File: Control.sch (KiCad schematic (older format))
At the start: 4 parts, among them J1 Conn_01x03_Female, J2 Conn_01x02_Female, U1 WeMos_mini, U19 BME280

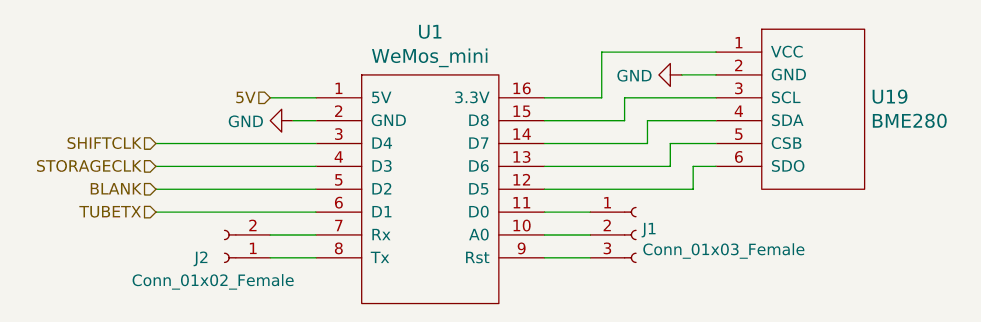
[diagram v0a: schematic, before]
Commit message: Fixed tube footprints and rerouted
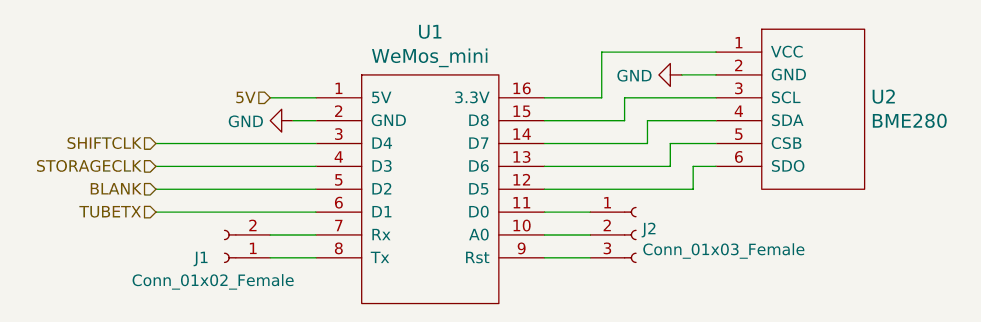
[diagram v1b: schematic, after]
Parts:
- U1: footprint BamboulabFootprints:D1_mini_board -> Bamboulibs:D1_mini_board
- renumbered J2 to J1, J1 to J2, U19 to U2
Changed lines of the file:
@@
 EESchema Schematic File Version 4
-LIBS:nixieClock_ZM1000-cache
 EELAYER 30 0
 EELAYER END
@@
 $EndDescr
 $Comp
-L nixieClock_ZM1000-rescue:WeMos_mini-bambouLab U1
+L nixieClock_ZM1000-rescue:WeMos_mini-bambouLab U?
 U 1 1 5D974EC7
 P 5700 4000
-AR Path="/5D974EC7" Ref="U1"  Part="1"
+AR Path="/5D974EC7" Ref="U?"  Part="1"
 AR Path="/5D9058C6/5D974EC7" Ref="U1"  Part="1"
 F 0 "U1" H 5700 4637 60  0000 C CNN
 F 1 "WeMos_mini" H 5700 4531 60  0000 C CNN
-F 2 "BamboulabFootprints:D1_mini_board" H 6250 3300 60  0001 C CNN
+F 2 "Bamboulibs:D1_mini_board" H 6250 3300 60  0001 C CNN
 F 3 "" H 5700 4531 60  0000 C CNN
 	1    5700 4000
@@
 	5000 3650 5200 3650
 $Comp
-L power:GND #PWR01
+L power:GND #PWR05
 U 1 1 5DBC6996
 P 5100 3750
-F 0 "#PWR01" H 5100 3500 50  0001 C CNN
+F 0 "#PWR05" H 5100 3500 50  0001 C CNN
 F 1 "GND" V 5105 3622 50  0000 R CNN
 F 2 "" H 5100 3750 50  0001 C CNN
@@
 	6200 4350 6400 4350
 $Comp
-L Connector:Conn_01x02_Female J2
+L Connector:Conn_01x02_Female J1
 U 1 1 5D97C070
 P 4800 4350
-F 0 "J2" H 4900 4350 50  0000 C CNN
+F 0 "J1" H 4900 4350 50  0000 C CNN
 F 1 "Conn_01x02_Female" H 4850 4450 50  0000 C CNN
 F 2 "Connector_PinHeader_2.54mm:PinHeader_1x02_P2.54mm_Vertical" H 4800 4350 50  0001 C CNN
@@
 	6200 4150 6400 4150
 $Comp
-L nixieClock_ZM1000-rescue:BME280-bambouLab U19
+L nixieClock_ZM1000-rescue:BME280-bambouLab U2
 U 1 1 5DA4BB9B
 P 7400 3800
-F 0 "U19" H 7628 3953 60  0000 L CNN
+F 0 "U2" H 7628 3953 60  0000 L CNN
 F 1 "BME280" H 7628 3847 60  0000 L CNN
 F 2 "nixies:BME280" H 7400 3800 60  0001 C CNN
@@
 	6950 3550 6800 3550
 $Comp
-L power:GND #PWR0106
+L power:GND #PWR06
 U 1 1 5DA50DD3
 P 6800 3550
-F 0 "#PWR0106" H 6800 3300 50  0001 C CNN
+F 0 "#PWR06" H 6800 3300 50  0001 C CNN
 F 1 "GND" V 6805 3422 50  0000 R CNN
 F 2 "" H 6800 3550 50  0001 C CNN
@@
 $EndComp
 $Comp
-L Connector:Conn_01x03_Female J1
+L Connector:Conn_01x03_Female J2
 U 1 1 5DA53641
 P 6600 4250
-F 0 "J1" H 6628 4276 50  0000 L CNN
+F 0 "J2" H 6628 4276 50  0000 L CNN
 F 1 "Conn_01x03_Female" H 6628 4185 50  0000 L CNN
 F 2 "Connector_PinHeader_2.54mm:PinHeader_1x03_P2.54mm_Vertical" H 6600 4250 50  0001 C CNN
